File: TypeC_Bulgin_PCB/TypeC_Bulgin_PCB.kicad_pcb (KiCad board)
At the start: 2 copper layers, 16.1 x 16.1 mm, 12 parts, among them J1 Conn_01x01_Female, J10 Conn_01x01_Female, J11 Conn_01x01_Female, J12 Conn_01x01_Female, J2 Conn_01x01_Female, J3 USB_C_Receptacle, J4 Conn_01x02_Female, J5 Conn_01x02_Female, J6 Conn_01x02_Female, J7 Conn_01x02_Female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

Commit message: v0.6 connectors prototype were added
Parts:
- removed J10, J11, J12, J8, J9: Conn_01x01_Female, Connector_PinHeader_1.00mm:PinHeader_1x01_P1.00mm_Vertical
- J3: value USB_C_Receptacle -> Conn_01x13; footprint Connector_USB:USB_C_Receptacle_JAE_DX07S024WJ3R400 -> Connector_Molex:Molex_Picoflex_90325-0014_2x07_P1.27mm_Vertical
- J4: value Conn_01x02_Female -> Conn_01x13; footprint Connector_PinHeader_1.00mm:PinHeader_1x02_P1.00mm_Vertical -> Connector_Molex:Molex_Picoflex_90325-0014_2x07_P1.27mm_Vertical
- J5: value Conn_01x02_Female -> Conn_02x10_Odd_Even; footprint Connector_PinHeader_1.00mm:PinHeader_1x02_P1.00mm_Vertical -> Connector_Molex:Molex_Picoflex_90325-0020_2x10_P1.27mm_Vertical
- J6: value Conn_01x02_Female -> USB_C_Receptacle; footprint Connector_PinHeader_1.00mm:PinHeader_1x02_P1.00mm_Vertical -> Connector_USB:USB_C_Receptacle_JAE_DX07S024WJ3R400
- J7: value Conn_01x02_Female -> Conn_01x01_Female; footprint Connector_PinHeader_1.00mm:PinHeader_1x02_P1.00mm_Vertical -> Connector_PinHeader_1.00mm:PinHeader_1x01_P1.00mm_Vertical
- moved J3 17.1 mm to (139.6, 99.9), turned to 90 degrees
- moved J7 7.01 mm to (145.8, 92.5), turned to 0 degrees
- moved J6 4.55 mm to (151.2, 87.5), turned to 0 degrees
- moved J4 4.37 mm to (151.2, 87.5), turned to 0 degrees
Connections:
- J4 pad 1: Net-(J3-PadB10) -> VBUS
- J4 pad 2: Net-(J3-PadB11) -> VBUS
- J5 pad 1: Net-(J3-PadA3) -> GND
- J5 pad 2: Net-(J3-PadA2) -> RX1-
- J7 pad 1: Net-(J3-PadB3) -> Net-(J6-PadS1)

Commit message: v0.8 ADT 13 pins was created
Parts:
- removed J1, J2, J7: Conn_01x01_Female, Connector_PinHeader_1.00mm:PinHeader_1x01_P1.00mm_Vertical
- removed J5: Conn_02x10_Odd_Even, Connector_Molex:Molex_Picoflex_90325-0020_2x10_P1.27mm_Vertical
- J3, J4: footprint Connector_Molex:Molex_Picoflex_90325-0014_2x07_P1.27mm_Vertical -> TypeC_Bulgin_PCB:ADT_13pin
- moved J3 18.9 mm to (147.4, 82.7)
- moved J4 6.31 mm to (147.5, 92.6), turned to 90 degrees
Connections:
- J6 pad A4: Net-(J1-Pad1) -> VBUS
- J6 pad A9: Net-(J1-Pad1) -> VBUS
- J6 pad B4: Net-(J1-Pad1) -> VBUS
- J6 pad B9: Net-(J1-Pad1) -> VBUS
- J6 pad S1: Net-(J6-PadS1) -> unconnected-(J6-PadS1)

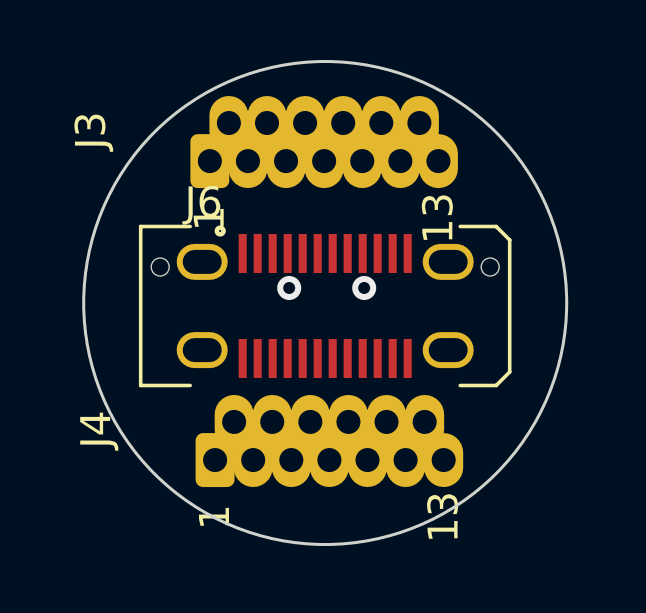
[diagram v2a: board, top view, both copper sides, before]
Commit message: v0.9 Land patterns were corrected
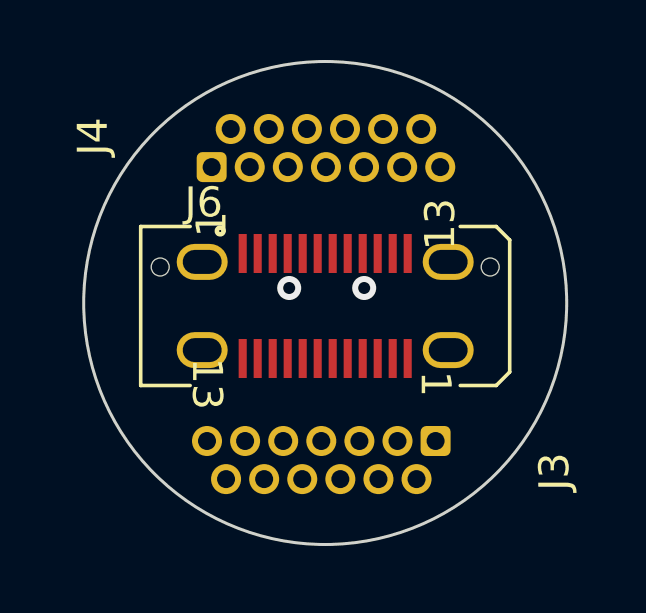
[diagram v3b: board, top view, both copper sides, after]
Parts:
- moved J3 12.0 mm to (154.9, 92.0), turned to -90 degrees
- moved J4 9.77 mm to (147.4, 82.9)
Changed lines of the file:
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@@
   )
   (footprint "TypeC_Bulgin_PCB:ADT_13pin" (layer "F.Cu")
-    (at 147.53 92.635 90)
+    (at 147.415 82.87 90)
     (descr "Molex Picoflex Ribbon-Cable Connectors, 90325-0014, 14 Pins (http://www.molex.com/pdm_docs/sd/903250004_sd.pdf), generated with kicad-footprint-generator")
     (tags "connector Molex Picoflex side entry")
@@
       (effects (font (size 1 1) (thickness 0.15)))
     )
-    (pad "1" thru_hole roundrect (at 0 0 90) (size 1.8 1.3) (drill 0.8) (layers *.Cu *.Mask) (roundrect_rratio 0.192308)
+    (pad "1" thru_hole roundrect (at 0 0 90) (size 1 1) (drill 0.6) (layers *.Cu *.Mask) (roundrect_rratio 0.192308)
       (net 8 "VBUS") (pinfunction "Pin_1") (pintype "passive"))
-    (pad "2" thru_hole oval (at 1.27 0.635 90) (size 1.8 1.3) (drill 0.8) (layers *.Cu *.Mask)
+    (pad "2" thru_hole oval (at 1.27 0.635 90) (size 1 1) (drill 0.6) (layers *.Cu *.Mask)
       (net 8 "VBUS") (pinfunction "Pin_2") (pintype "passive"))
-    (pad "3" thru_hole oval (at 0 1.27 90) (size 1.8 1.3) (drill 0.8) (layers *.Cu *.Mask)
+    (pad "3" thru_hole oval (at 0 1.27 90) (size 1 1) (drill 0.6) (layers *.Cu *.Mask)
       (net 14 "unconnected-(J4-Pad3)") (pinfunction "Pin_3") (pintype "passive"))
-    (pad "4" thru_hole oval (at 1.27 1.905 90) (size 1.8 1.3) (drill 0.8) (layers *.Cu *.Mask)
+    (pad "4" thru_hole oval (at 1.27 1.905 90) (size 1 1) (drill 0.6) (layers *.Cu *.Mask)
       (net 1 "GND") (pinfunction "Pin_4") (pintype "passive"))
-    (pad "5" thru_hole oval (at 0 2.54 90) (size 1.8 1.3) (drill 0.8) (layers *.Cu *.Mask)
+    (pad "5" thru_hole oval (at 0 2.54 90) (size 1 1) (drill 0.6) (layers *.Cu *.Mask)
       (net 12 "TX2+") (pinfunction "Pin_5") (pintype "passive"))
-    (pad "6" thru_hole oval (at 1.27 3.175 90) (size 1.8 1.3) (drill 0.8) (layers *.Cu *.Mask)
+    (pad "6" thru_hole oval (at 1.27 3.175 90) (size 1 1) (drill 0.6) (layers *.Cu *.Mask)
       (net 11 "TX2-") (pinfunction "Pin_6") (pintype "passive"))
-    (pad "7" thru_hole oval (at 0 3.81 90) (size 1.8 1.3) (drill 0.8) (layers *.Cu *.Mask)
+    (pad "7" thru_hole oval (at 0 3.81 90) (size 1 1) (drill 0.6) (layers *.Cu *.Mask)
       (net 1 "GND") (pinfunction "Pin_7") (pintype "passive"))
-    (pad "8" thru_hole oval (at 1.27 4.445 90) (size 1.8 1.3) (drill 0.8) (layers *.Cu *.Mask)
+    (pad "8" thru_hole oval (at 1.27 4.445 90) (size 1 1) (drill 0.6) (layers *.Cu *.Mask)
       (net 15 "unconnected-(J4-Pad8)") (pinfunction "Pin_8") (pintype "passive"))
-    (pad "9" thru_hole oval (at 0 5.08 90) (size 1.8 1.3) (drill 0.8) (layers *.Cu *.Mask)
+    (pad "9" thru_hole oval (at 0 5.08 90) (size 1 1) (drill 0.6) (layers *.Cu *.Mask)
       (net 16 "unconnected-(J4-Pad9)") (pinfunction "Pin_9") (pintype "passive"))
-    (pad "10" thru_hole oval (at 1.27 5.715 90) (size 1.8 1.3) (drill 0.8) (layers *.Cu *.Mask)
+    (pad "10" thru_hole oval (at 1.27 5.715 90) (size 1 1) (drill 0.6) (layers *.Cu *.Mask)
       (net 1 "GND") (pinfunction "Pin_10") (pintype "passive"))
-    (pad "11" thru_hole oval (at 0 6.35 90) (size 1.8 1.3) (drill 0.8) (layers *.Cu *.Mask)
+    (pad "11" thru_hole oval (at 0 6.35 90) (size 1 1) (drill 0.6) (layers *.Cu *.Mask)
       (net 10 "RX2+") (pinfunction "Pin_11") (pintype "passive"))
-    (pad "12" thru_hole oval (at 1.27 6.985 90) (size 1.8 1.3) (drill 0.8) (layers *.Cu *.Mask)
+    (pad "12" thru_hole oval (at 1.27 6.985 90) (size 1 1) (drill 0.6) (layers *.Cu *.Mask)
       (net 9 "RX2-") (pinfunction "Pin_12") (pintype "passive"))
-    (pad "13" thru_hole oval (at 0 7.62 90) (size 1.8 1.3) (drill 0.8) (layers *.Cu *.Mask)
+    (pad "13" thru_hole oval (at 0 7.62 90) (size 1 1) (drill 0.6) (layers *.Cu *.Mask)
       (net 1 "GND") (pinfunction "Pin_13") (pintype "passive"))
     (model "${KICAD6_3DMODEL_DIR}/Connector_Molex.3dshapes/Molex_Picoflex_90325-0014_2x07_P1.27mm_Vertical.wrl"
@@
   )
   (footprint "TypeC_Bulgin_PCB:ADT_13pin" (layer "F.Cu")
-    (at 147.355 82.67 90)
+    (at 154.88 92 -90)
     (descr "Molex Picoflex Ribbon-Cable Connectors, 90325-0014, 14 Pins (http://www.molex.com/pdm_docs/sd/903250004_sd.pdf), generated with kicad-footprint-generator")
     (tags "connector Molex Picoflex side entry")
@@
       (effects (font (size 1 1) (thickness 0.15)))
     )
-    (fp_text user "13" (at -1.905 7.62 90 unlocked) (layer "F.SilkS")
+    (fp_text user "1" (at -1.905 0 -90 unlocked) (layer "F.SilkS")
       (effects (font (size 1 1) (thickness 0.15)))
     )
-    (fp_text user "1" (at -1.905 0 90 unlocked) (layer "F.SilkS")
+    (fp_text user "13" (at -1.905 7.62 -90 unlocked) (layer "F.SilkS")
       (effects (font (size 1 1) (thickness 0.15)))
     )
@@
       (effects (font (size 1 1) (thickness 0.15)))
     )
-    (pad "1" thru_hole roundrect (at 0 0 90) (size 1.8 1.3) (drill 0.8) (layers *.Cu *.Mask) (roundrect_rratio 0.192308)
+    (pad "1" thru_hole roundrect (at 0 0 270) (size 1 1) (drill 0.6) (layers *.Cu *.Mask) (roundrect_rratio 0.192308)
       (net 8 "VBUS") (pinfunction "Pin_1") (pintype "passive"))
-    (pad "2" thru_hole oval (at 1.27 0.635 90) (size 1.8 1.3) (drill 0.8) (layers *.Cu *.Mask)
+    (pad "2" thru_hole oval (at 1.27 0.635 270) (size 1 1) (drill 0.6) (layers *.Cu *.Mask)
       (net 8 "VBUS") (pinfunction "Pin_2") (pintype "passive"))
-    (pad "3" thru_hole oval (at 0 1.27 90) (size 1.8 1.3) (drill 0.8) (layers *.Cu *.Mask)
+    (pad "3" thru_hole oval (at 0 1.27 270) (size 1 1) (drill 0.6) (layers *.Cu *.Mask)
       (net 13 "unconnected-(J3-Pad3)") (pinfunction "Pin_3") (pintype "passive"))
-    (pad "4" thru_hole oval (at 1.27 1.905 90) (size 1.8 1.3) (drill 0.8) (layers *.Cu *.Mask)
+    (pad "4" thru_hole oval (at 1.27 1.905 270) (size 1 1) (drill 0.6) (layers *.Cu *.Mask)
       (net 1 "GND") (pinfunction "Pin_4") (pintype "passive"))
-    (pad "5" thru_hole oval (at 0 2.54 90) (size 1.8 1.3) (drill 0.8) (layers *.Cu *.Mask)
+    (pad "5" thru_hole oval (at 0 2.54 270) (size 1 1) (drill 0.6) (layers *.Cu *.Mask)
       (net 5 "TX1+") (pinfunction "Pin_5") (pintype "passive"))
-    (pad "6" thru_hole oval (at 1.27 3.175 90) (size 1.8 1.3) (drill 0.8) (layers *.Cu *.Mask)
+    (pad "6" thru_hole oval (at 1.27 3.175 270) (size 1 1) (drill 0.6) (layers *.Cu *.Mask)
       (net 4 "TX1-") (pinfunction "Pin_6") (pintype "passive"))
-    (pad "7" thru_hole oval (at 0 3.81 90) (size 1.8 1.3) (drill 0.8) (layers *.Cu *.Mask)
+    (pad "7" thru_hole oval (at 0 3.81 270) (size 1 1) (drill 0.6) (layers *.Cu *.Mask)
       (net 1 "GND") (pinfunction "Pin_7") (pintype "passive"))
-    (pad "8" thru_hole oval (at 1.27 4.445 90) (size 1.8 1.3) (drill 0.8) (layers *.Cu *.Mask)
+    (pad "8" thru_hole oval (at 1.27 4.445 270) (size 1 1) (drill 0.6) (layers *.Cu *.Mask)
       (net 6 "unconnected-(J3-Pad8)") (pinfunction "Pin_8") (pintype "passive"))
-    (pad "9" thru_hole oval (at 0 5.08 90) (size 1.8 1.3) (drill 0.8) (layers *.Cu *.Mask)
+    (pad "9" thru_hole oval (at 0 5.08 270) (size 1 1) (drill 0.6) (layers *.Cu *.Mask)
       (net 7 "unconnected-(J3-Pad9)") (pinfunction "Pin_9") (pintype "passive"))
-    (pad "10" thru_hole oval (at 1.27 5.715 90) (size 1.8 1.3) (drill 0.8) (layers *.Cu *.Mask)
+    (pad "10" thru_hole oval (at 1.27 5.715 270) (size 1 1) (drill 0.6) (layers *.Cu *.Mask)
       (net 1 "GND") (pinfunction "Pin_10") (pintype "passive"))
-    (pad "11" thru_hole oval (at 0 6.35 90) (size 1.8 1.3) (drill 0.8) (layers *.Cu *.Mask)
+    (pad "11" thru_hole oval (at 0 6.35 270) (size 1 1) (drill 0.6) (layers *.Cu *.Mask)
       (net 3 "RX1+") (pinfunction "Pin_11") (pintype "passive"))
-    (pad "12" thru_hole oval (at 1.27 6.985 90) (size 1.8 1.3) (drill 0.8) (layers *.Cu *.Mask)
+    (pad "12" thru_hole oval (at 1.27 6.985 270) (size 1 1) (drill 0.6) (layers *.Cu *.Mask)
       (net 2 "RX1-") (pinfunction "Pin_12") (pintype "passive"))
-    (pad "13" thru_hole oval (at 0 7.62 90) (size 1.8 1.3) (drill 0.8) (layers *.Cu *.Mask)
+    (pad "13" thru_hole oval (at 0 7.62 270) (size 1 1) (drill 0.6) (layers *.Cu *.Mask)
       (net 1 "GND") (pinfunction "Pin_13") (pintype "passive"))
     (model "${KICAD6_3DMODEL_DIR}/Connector_Molex.3dshapes/Molex_Picoflex_90325-0014_2x07_P1.27mm_Vertical.wrl"

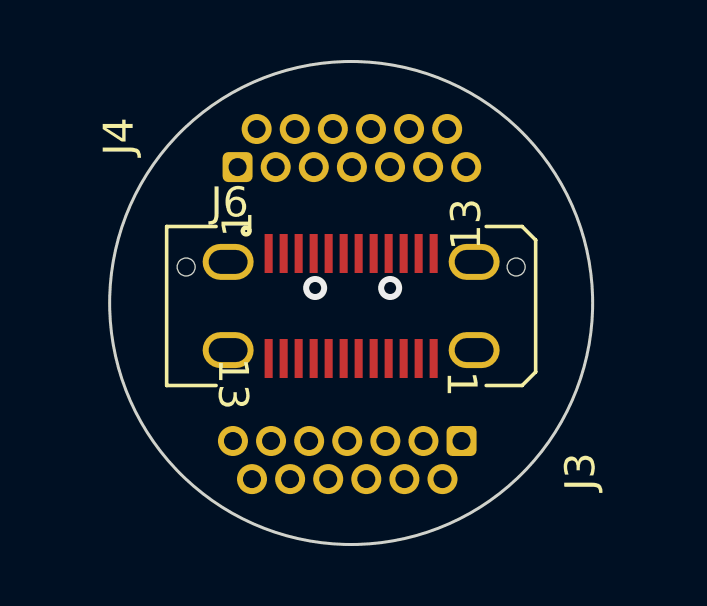
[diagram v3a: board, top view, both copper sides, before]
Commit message: v0.91 circuit was corrected
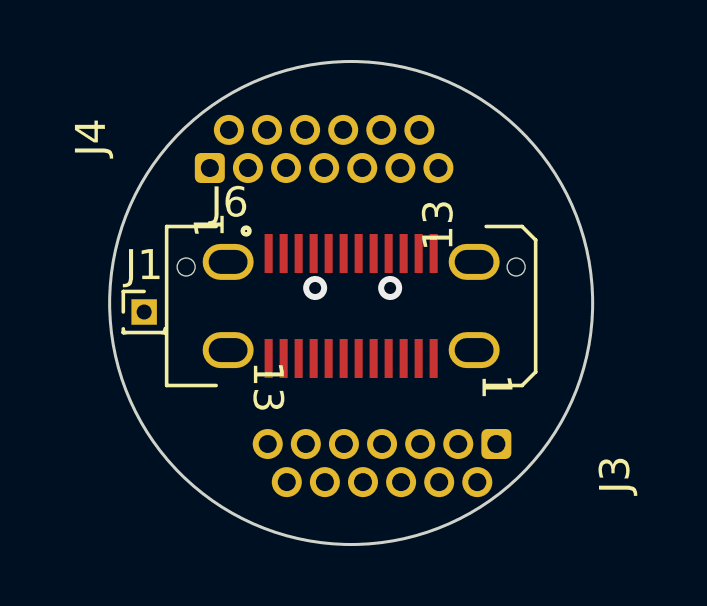
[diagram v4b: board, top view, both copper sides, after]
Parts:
- added J1: Conn_01x01_Female, Connector_PinHeader_1.00mm:PinHeader_1x01_P1.00mm_Vertical, F.Cu at (144.3, 87.7)
- moved J3 1.16 mm to (156.0, 92.1)
- moved J4 0.93 mm to (146.5, 82.9)
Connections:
- J3 pad 11: RX1+ -> RX1-
- J3 pad 12: RX1- -> RX1+
- J4 pad 11: RX2+ -> RX2-
- J4 pad 12: RX2- -> RX2+
- J6 pad A2: TX1+ -> TX2+
- J6 pad A3: TX1- -> TX2-
- J6 pad B2: TX2+ -> TX1+
- J6 pad B3: TX2- -> TX1-
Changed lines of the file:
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@@
   (net 24 "unconnected-(J6-PadB7)")
   (net 25 "unconnected-(J6-PadB8)")
+  (net 26 "unconnected-(J1-Pad1)")
   (footprint "Connector_USB:USB_C_Receptacle_JAE_DX07S024WJ3R400" (layer "F.Cu")
     (at 151.2 87.5)
@@
       (net 1 "GND") (pinfunction "GND") (pintype "passive"))
     (pad "A2" smd rect (at -2.25 -1.75) (size 0.27 1.3) (layers "F.Cu" "F.Paste" "F.Mask")
-      (net 5 "TX1+") (pinfunction "TX1+") (pintype "bidirectional"))
+      (net 12 "TX2+") (pinfunction "TX1+") (pintype "bidirectional"))
     (pad "A3" smd rect (at -1.75 -1.75) (size 0.27 1.3) (layers "F.Cu" "F.Paste" "F.Mask")
-      (net 4 "TX1-") (pinfunction "TX1-") (pintype "bidirectional"))
+      (net 11 "TX2-") (pinfunction "TX1-") (pintype "bidirectional"))
     (pad "A4" smd rect (at -1.25 -1.75) (size 0.27 1.3) (layers "F.Cu" "F.Paste" "F.Mask")
       (net 8 "VBUS") (pinfunction "VBUS") (pintype "passive"))
@@
       (net 1 "GND") (pinfunction "GND") (pintype "passive"))
     (pad "B2" smd rect (at 2.25 1.75) (size 0.27 1.3) (layers "F.Cu" "F.Paste" "F.Mask")
-      (net 12 "TX2+") (pinfunction "TX2+") (pintype "bidirectional"))
+      (net 5 "TX1+") (pinfunction "TX2+") (pintype "bidirectional"))
     (pad "B3" smd rect (at 1.75 1.75) (size 0.27 1.3) (layers "F.Cu" "F.Paste" "F.Mask")
-      (net 11 "TX2-") (pinfunction "TX2-") (pintype "bidirectional"))
+      (net 4 "TX1-") (pinfunction "TX2-") (pintype "bidirectional"))
     (pad "B4" smd rect (at 1.25 1.75) (size 0.27 1.3) (layers "F.Cu" "F.Paste" "F.Mask")
       (net 8 "VBUS") (pinfunction "VBUS") (pintype "passive"))
@@
   )
   (footprint "TypeC_Bulgin_PCB:ADT_13pin" (layer "F.Cu")
-    (at 147.415 82.87 90)
+    (at 146.49 82.9 90)
     (descr "Molex Picoflex Ribbon-Cable Connectors, 90325-0014, 14 Pins (http://www.molex.com/pdm_docs/sd/903250004_sd.pdf), generated with kicad-footprint-generator")
     (tags "connector Molex Picoflex side entry")
@@
       (net 1 "GND") (pinfunction "Pin_10") (pintype "passive"))
     (pad "11" thru_hole oval (at 0 6.35 90) (size 1 1) (drill 0.6) (layers *.Cu *.Mask)
-      (net 10 "RX2+") (pinfunction "Pin_11") (pintype "passive"))
+      (net 9 "RX2-") (pinfunction "Pin_11") (pintype "passive"))
     (pad "12" thru_hole oval (at 1.27 6.985 90) (size 1 1) (drill 0.6) (layers *.Cu *.Mask)
-      (net 9 "RX2-") (pinfunction "Pin_12") (pintype "passive"))
+      (net 10 "RX2+") (pinfunction "Pin_12") (pintype "passive"))
     (pad "13" thru_hole oval (at 0 7.62 90) (size 1 1) (drill 0.6) (layers *.Cu *.Mask)
       (net 1 "GND") (pinfunction "Pin_13") (pintype "passive"))
@@
   )
   (footprint "TypeC_Bulgin_PCB:ADT_13pin" (layer "F.Cu")
-    (at 154.88 92 -90)
+    (at 156.04 92.1 -90)
     (descr "Molex Picoflex Ribbon-Cable Connectors, 90325-0014, 14 Pins (http://www.molex.com/pdm_docs/sd/903250004_sd.pdf), generated with kicad-footprint-generator")
     (tags "connector Molex Picoflex side entry")
@@
       (net 1 "GND") (pinfunction "Pin_10") (pintype "passive"))
     (pad "11" thru_hole oval (at 0 6.35 270) (size 1 1) (drill 0.6) (layers *.Cu *.Mask)
-      (net 3 "RX1+") (pinfunction "Pin_11") (pintype "passive"))
+      (net 2 "RX1-") (pinfunction "Pin_11") (pintype "passive"))
     (pad "12" thru_hole oval (at 1.27 6.985 270) (size 1 1) (drill 0.6) (layers *.Cu *.Mask)
-      (net 2 "RX1-") (pinfunction "Pin_12") (pintype "passive"))
+      (net 3 "RX1+") (pinfunction "Pin_12") (pintype "passive"))
     (pad "13" thru_hole oval (at 0 7.62 270) (size 1 1) (drill 0.6) (layers *.Cu *.Mask)
       (net 1 "GND") (pinfunction "Pin_13") (pintype "passive"))
@@
       (offset (xyz 0 0 0))
       (scale (xyz 1 1 1))
+      (rotate (xyz 0 0 0))
+    )
+  )
+  (footprint "Connector_PinHeader_1.00mm:PinHeader_1x01_P1.00mm_Vertical" (layer "F.Cu")
+    (at 144.3 87.7)
+    (descr "Through hole straight pin header, 1x01, 1.00mm pitch, single row")
+    (tags "Through hole pin header THT 1x01 1.00mm single row")
+    (property "Sheetfile" "TypeC_Bulgin_PCB.kicad_sch")
+    (property "Sheetname" "")
+    (attr through_hole)
+    (fp_text reference "J1" (at 0 -1.56) (layer "F.SilkS")
+      (effects (font (size 1 1) (thickness 0.15)))
+    )
+    (fp_text value "Conn_01x01_Female" (at 0 1.56) (layer "F.Fab")
+      (effects (font (size 1 1) (thickness 0.15)))
+    )
+    (fp_text user "${REFERENCE}" (at 0 0 90) (layer "F.Fab")
+      (effects (font (size 0.76 0.76) (thickness 0.114)))
+    )
+    (fp_line (start -0.695 0.685) (end -0.695 0.56) (layer "F.SilkS") (width 0.12))
+    (fp_line (start -0.695 0) (end -0.695 -0.685) (layer "F.SilkS") (width 0.12))
+    (fp_line (start -0.695 0.685) (end -0.608276 0.685) (layer "F.SilkS") (width 0.12))
+    (fp_line (start 0.695 0.685) (end 0.695 0.56) (layer "F.SilkS") (width 0.12))
+    (fp_line (start 0.608276 0.685) (end 0.695 0.685) (layer "F.SilkS") (width 0.12))
+    (fp_line (start -0.695 0.685) (end 0.695 0.685) (layer "F.SilkS") (width 0.12))
+    (fp_line (start -0.695 -0.685) (end 0 -0.685) (layer "F.SilkS") (width 0.12))
+    (fp_line (start -1.15 -1) (end -1.15 1) (layer "F.CrtYd") (width 0.05))
+    (fp_line (start 1.15 1) (end 1.15 -1) (layer "F.CrtYd") (width 0.05))
+    (fp_line (start -1.15 1) (end 1.15 1) (layer "F.CrtYd") (width 0.05))
+    (fp_line (start 1.15 -1) (end -1.15 -1) (layer "F.CrtYd") (width 0.05))
+    (fp_line (start -0.3175 -0.5) (end 0.635 -0.5) (layer "F.Fab") (width 0.1))
+    (fp_line (start 0.635 0.5) (end -0.635 0.5) (layer "F.Fab") (width 0.1))
+    (fp_line (start -0.635 0.5) (end -0.635 -0.1825) (layer "F.Fab") (width 0.1))
+    (fp_line (start -0.635 -0.1825) (end -0.3175 -0.5) (layer "F.Fab") (width 0.1))
+    (fp_line (start 0.635 -0.5) (end 0.635 0.5) (layer "F.Fab") (width 0.1))
+    (pad "1" thru_hole rect (at 0 0) (size 0.85 0.85) (drill 0.5) (layers *.Cu *.Mask)
+      (net 26 "unconnected-(J1-Pad1)") (pinfunction "Pin_1") (pintype "passive"))
+    (model "${KICAD6_3DMODEL_DIR}/Connector_PinHeader_1.00mm.3dshapes/PinHeader_1x01_P1.00mm_Vertical.wrl"
+      (offset (xyz 0 0 0))
+      (scale (xyz 1 1 1))

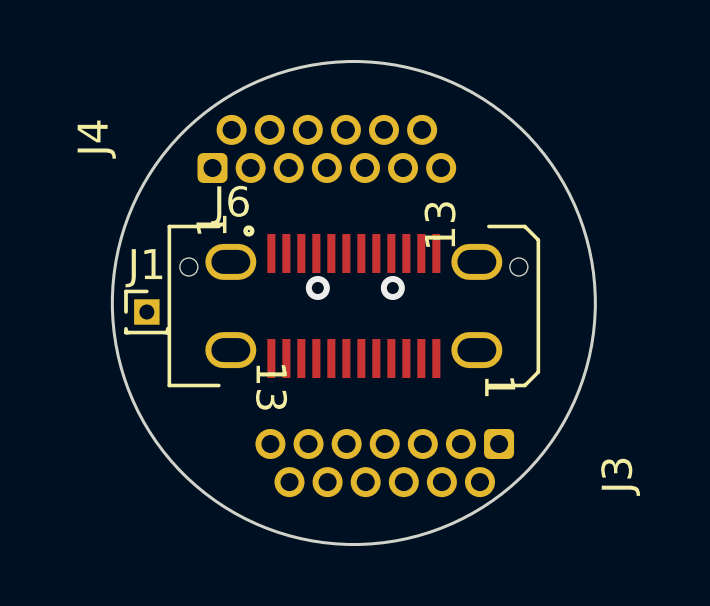
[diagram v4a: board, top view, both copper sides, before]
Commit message: v0.92 land patterns of ADT13pins were corrected
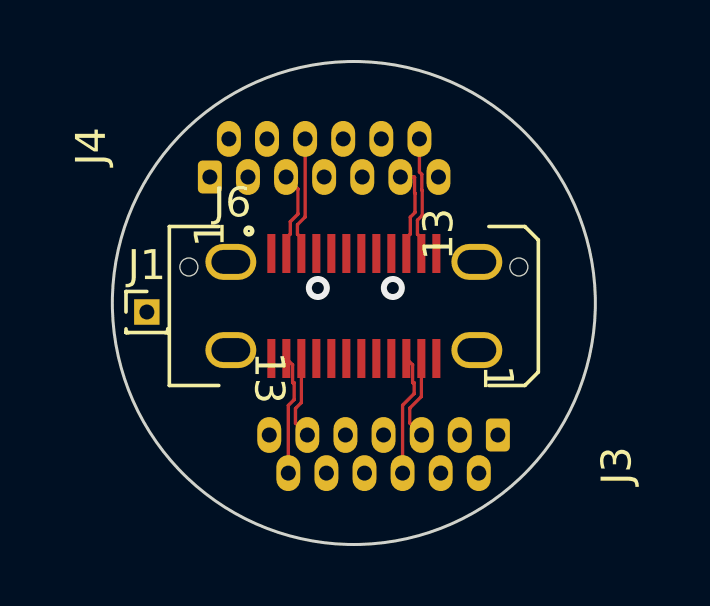
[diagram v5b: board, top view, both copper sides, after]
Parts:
- moved J4 0.31 mm to (146.4, 83.2)
- moved J3 0.30 mm to (156.0, 91.8)
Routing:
- net TX1-: track 0.00 -> 4.12 mm
- net RX1+: track 0.00 -> 4.04 mm
- net TX2-: track 0.00 -> 3.98 mm
- net RX2+: track 0.00 -> 3.98 mm
- net RX2-: track 0.00 -> 3.15 mm
- net TX1+: track 0.00 -> 2.87 mm
- net TX2+: track 0.00 -> 2.87 mm
- net RX1-: track 0.00 -> 2.80 mm
